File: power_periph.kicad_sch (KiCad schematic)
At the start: 6 parts, among them J6 UART_GPS, J7 UART_ELRS, J9 I2C_MAG

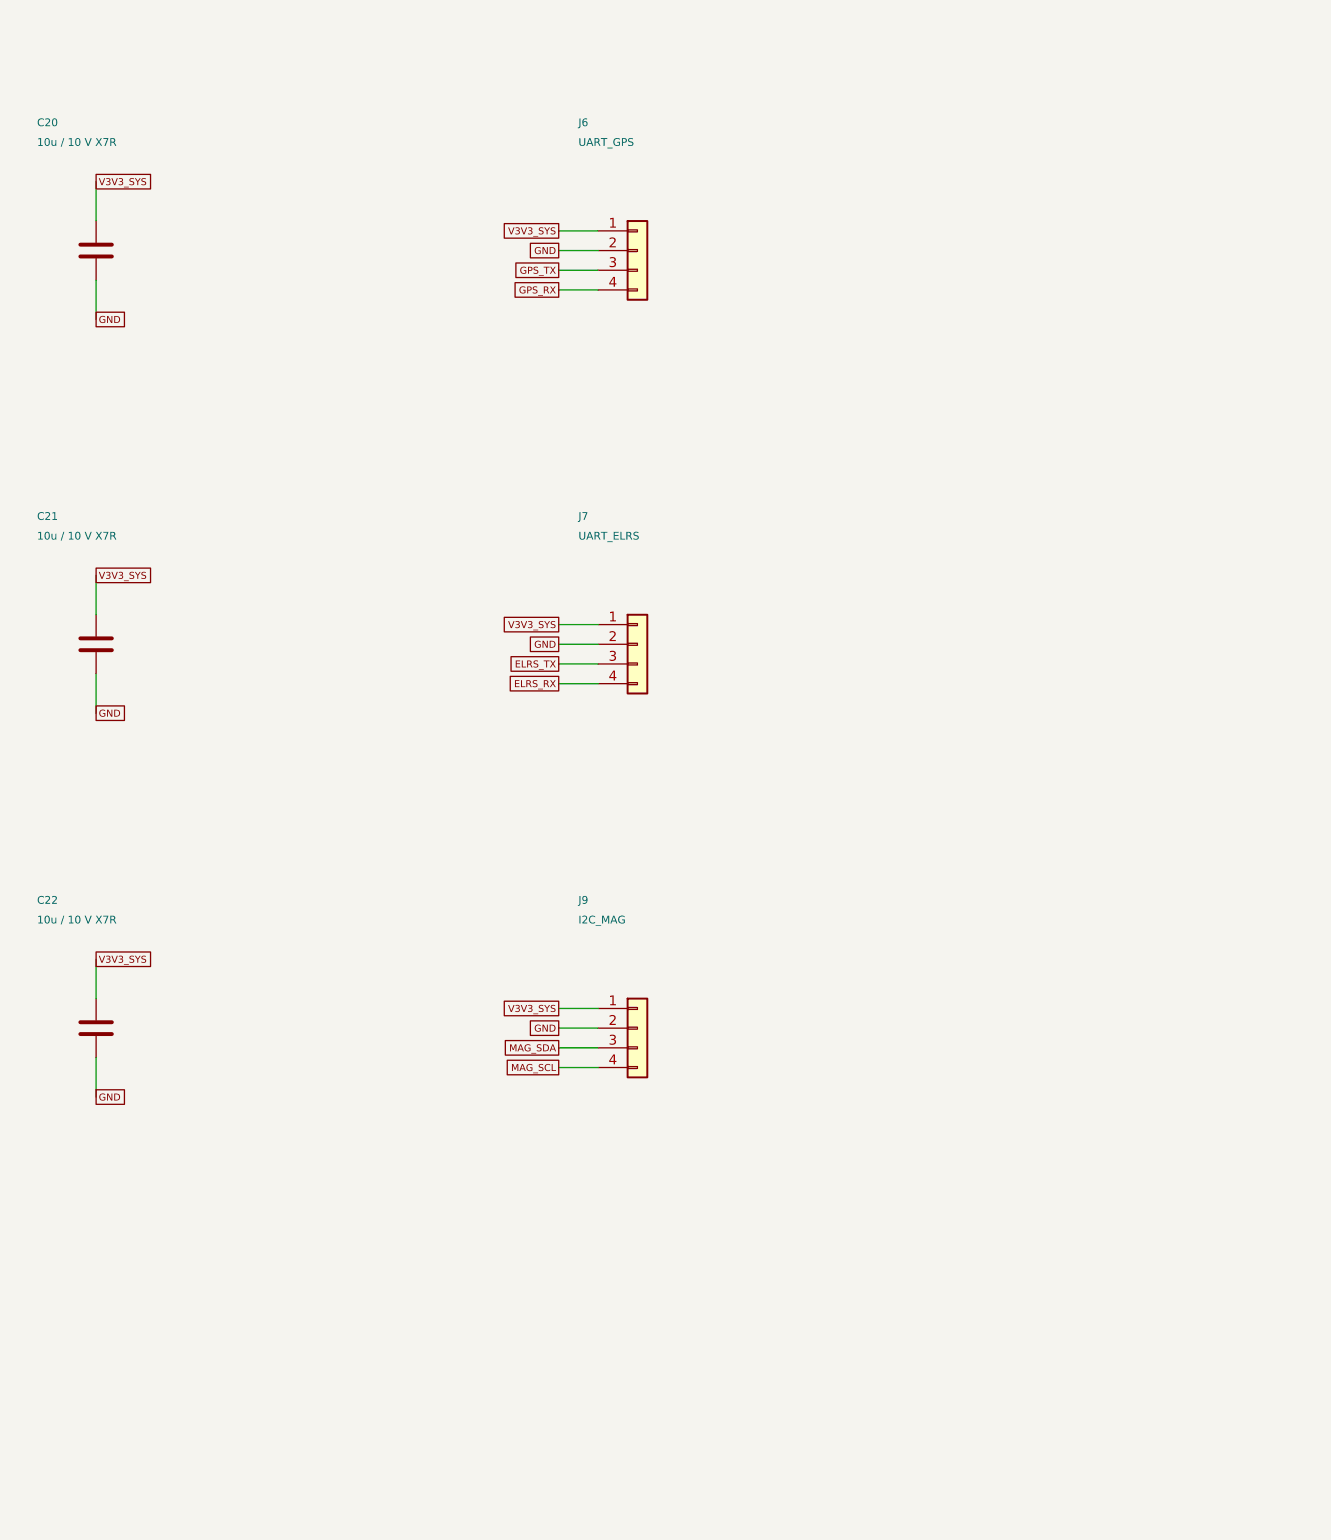
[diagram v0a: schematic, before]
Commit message: Schematic review: TPS2121 input stage, DS-009 ports, sequencing and CS fixes; docs trimmed
Datasheet-grounded review of the full flight-controller schematic. Downstream
of the input everything verified pin-by-pin (TPS62913, TPS7A20, RP2354B,
BMI088/BMP581/ADXL375, W25Q128, microSD, PWM). The 5 V input stage did not:

- LM66100 (5.5 V rec-op / 6 V abs-max) replaced by one TPS2121 mux (U25):
  BEC priority on IN1, OV lockout ~5.86 V, current limit ~1.5 A, reverse
  blocking on both inputs, source status on GPIO39. Input spec 4.75-5.5 V.
- 5V_IN: 2x4.7 uF + 100 uF + SMAJ5.0A TVS; J3 JST-XH -> XT30PW-M (pin 1 GND).
- J6/J7/J9 reordered to Pixhawk DS-009 (VCC/sig/sig/GND); GPS/ELRS VCC 5 V.
- VIN_SENSE 22k/10k (full scale 10.6 V, was saturating at 5.5 V).
- TPS7A20 EN <- PWR_GOOD so V3V3_ANA rises after V3V3_SYS.
- RP2354B VREG_AVDD moved to V3V3_SYS (datasheet 6.1.8: must power up with
  VREG_VIN); ADC_AVDD stays on V3V3_ANA.
- 10k pull-ups on the four sensor chip-selects.
- ERC "global label appears once" re-enabled (0 hits).

Generator, netlist checker and SPICE decks updated (TPS2121 behavioral model,
new over-voltage and 2S mis-plug corners). Build idempotent, 143 pin mappings
PASS, ERC 0/0, all corners PASS.

Docs: POWER_*.md history removed, rationale folded into DESIGN_SPEC Decisions;
808 -> 290 lines across README, DESIGN_SPEC, LIBRARIES, simulations/README.

Co-Authored-By: Claude Fable 5.1 <noreply@anthropic.com>
Claude-Session: https://claude.ai/code/session_015cFNiWgf35VN2T43HaK8PE
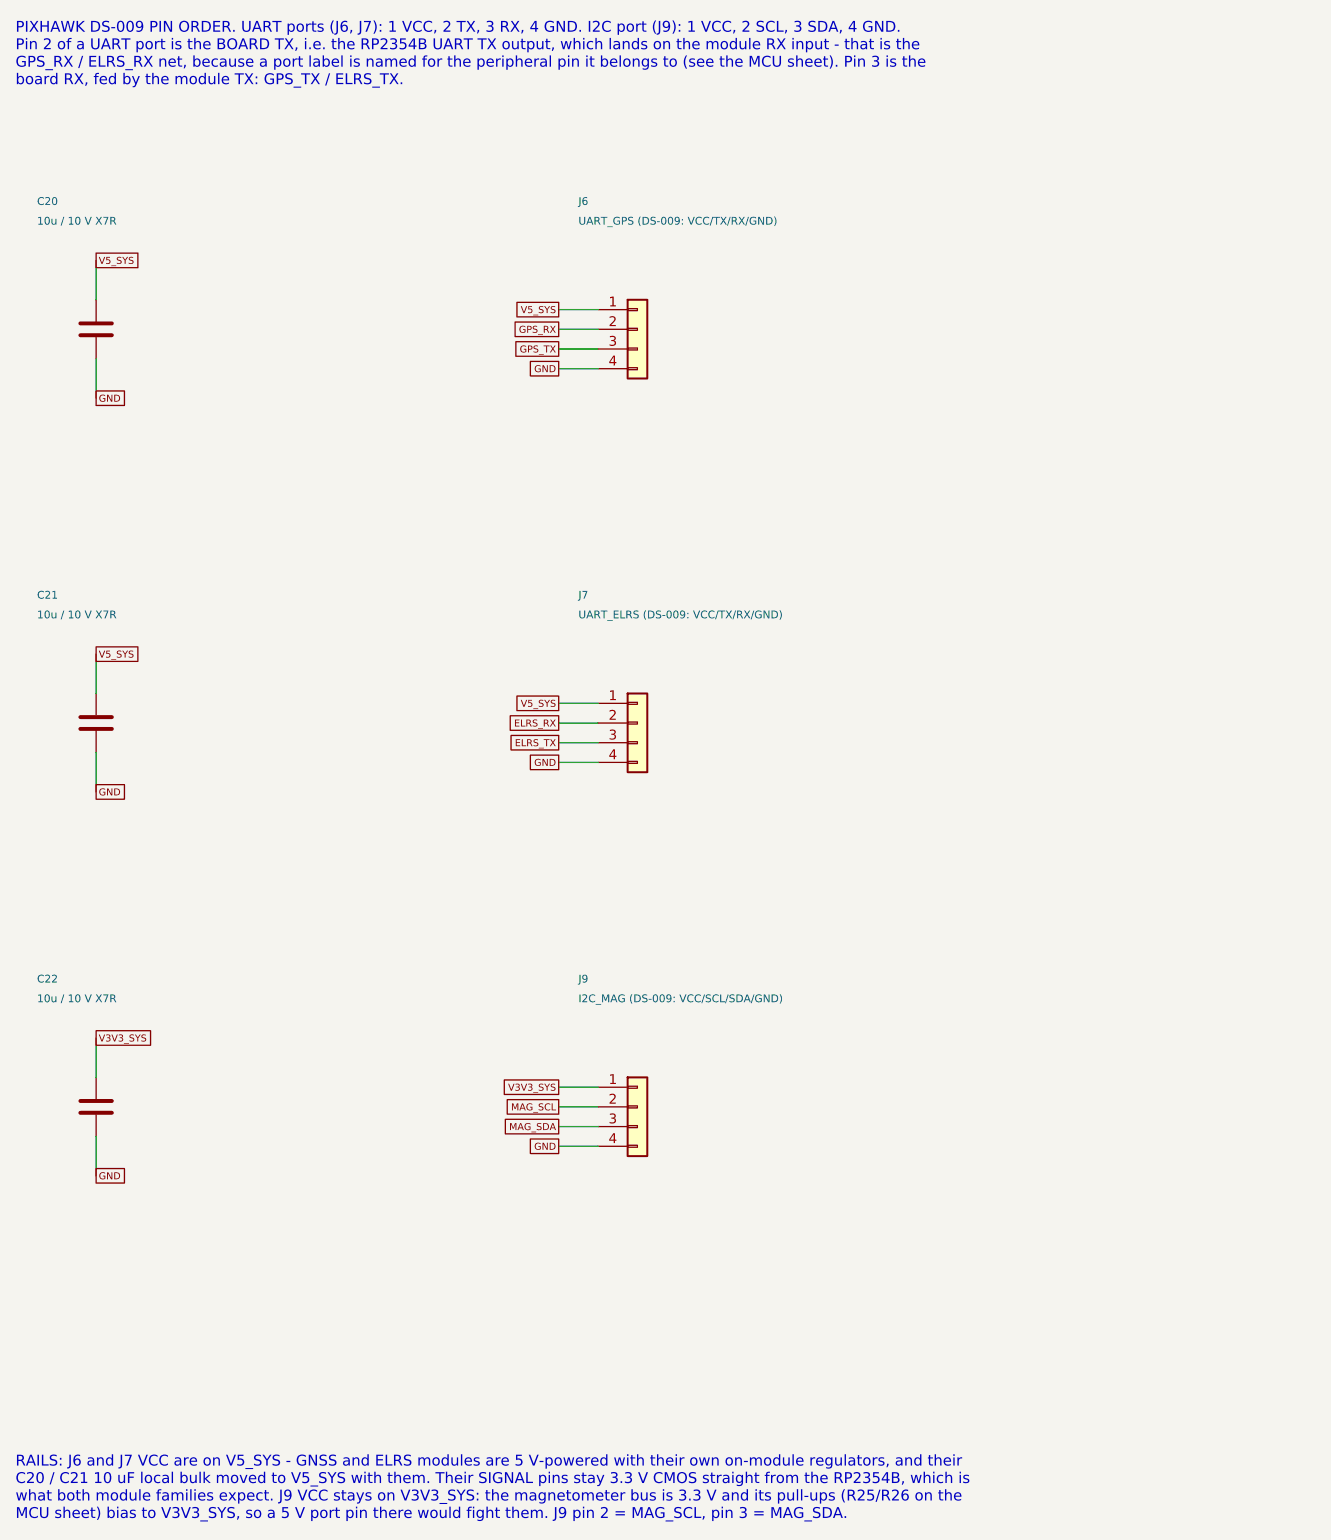
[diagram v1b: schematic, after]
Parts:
- J6: value UART_GPS -> UART_GPS (DS-009: VCC/TX/RX/GND)
- J7: value UART_ELRS -> UART_ELRS (DS-009: VCC/TX/RX/GND)
- J9: value I2C_MAG -> I2C_MAG (DS-009: VCC/SCL/SDA/GND)
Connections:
- net ELRS_RX: now also J7.2 (Pin_2); no longer J7.4 (Pin_4)
- net GND: now also J6.4 (Pin_4), J7.4 (Pin_4), J9.4 (Pin_4); no longer J6.2 (Pin_2), J7.2 (Pin_2), J9.2 (Pin_2)
- net GPS_RX: now also J6.2 (Pin_2); no longer J6.4 (Pin_4)
- net MAG_SCL: now also J9.2 (Pin_2); no longer J9.4 (Pin_4)
- net V3V3_SYS: no longer C20.1, C21.1, J6.1 (Pin_1), J7.1 (Pin_1)
- new net V5_SYS: C20.1, C21.1, J6.1 (Pin_1), J7.1 (Pin_1)
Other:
- note added: "PIXHAWK DS-009 PIN ORDER. UART ports (J6, J7): 1 VCC, 2 TX, 3 RX, 4 GND. I2C port (J9): 1 VCC, 2 SCL, 3 SDA, 4 GND. Pin 2 of a UART port is the BOARD TX, i.e. the RP2354B UART TX output, which lands on the module RX input - that is the GPS_RX / ELRS_RX net, because a port label is named for the peripheral pin it belongs to (see the MCU sheet). Pin 3 is the board RX, fed by the module TX: GPS_TX /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"
- note added: "RAILS: J6 and J7 VCC are on V5_SYS - GNSS and ELRS modules are 5 V-powered with their own on-module regulators, and their C20 / C21 10 uF local bulk moved to V5_SYS with them. Their SIGNAL pins stay 3.3 V CMOS straight from the RP2354B, which is what both module families expect. J9 VCC stays on V3V3_SYS: the magnetometer bus is 3.3 V and its pull-ups (R25/R26 on the MCU sheet) bias to V3V3_SYS, s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"
- moved on the sheet: C20, C21, C22, J6, J7, J9

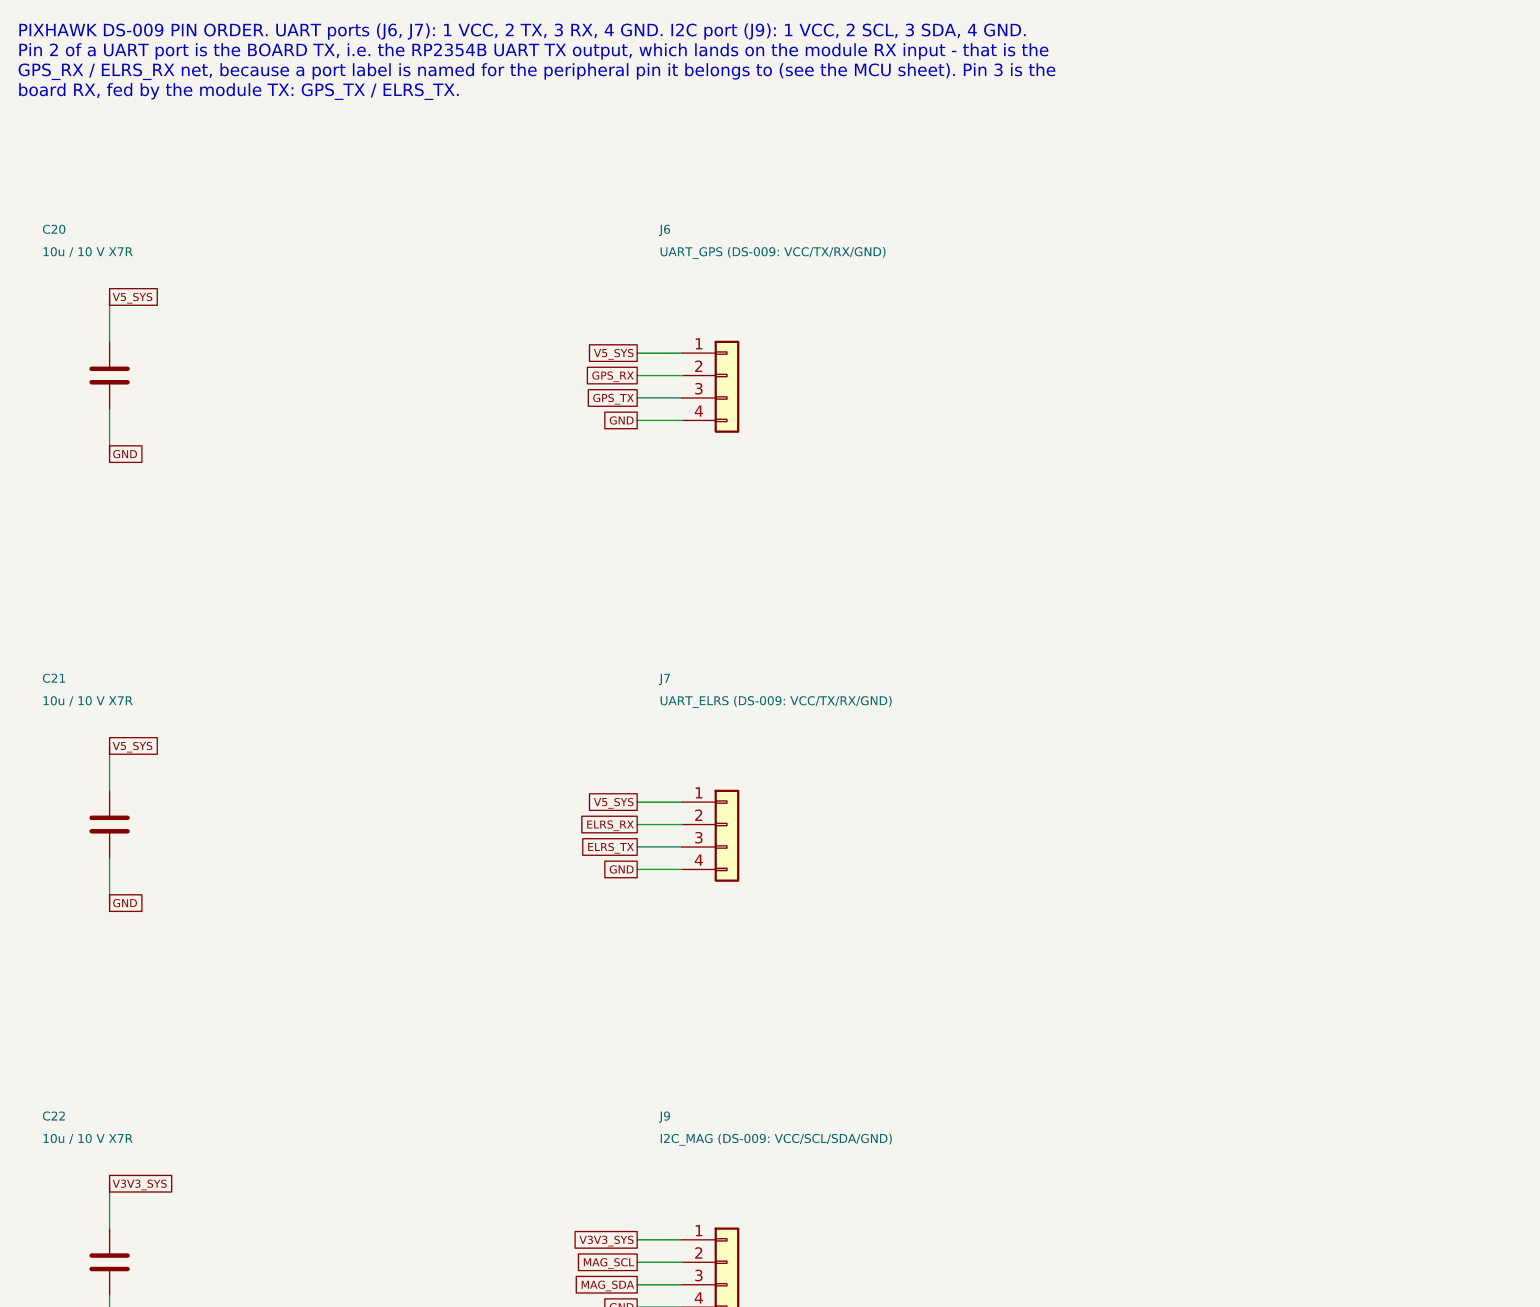
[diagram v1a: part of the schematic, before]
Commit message: Physical design: VBAT-in buck, ESC pad row, pad-row IO, 50 mm single-sided board
Power: the FC now takes raw 2-6S VBAT from the MicoAir AM32 4-in-1 ESC pad
row (CURR TX M4 M3 M2 M1 VBAT GND, J3) through an AP63205WU 5 V/2 A buck
(U26, XGL4030-472, 3 x 22 uF) into the existing TPS2121 mux; XT30 and its
TVS removed. VBAT sense 100k/10k (36 V FS) on ADC0, ESC current sense on
ADC2, ESC KISS telemetry on GPIO30.

IO per the physical spec (DESIGN_SPEC "Physical design"): solder pad rows
for GPS/ELRS/MAG (JST-GH removed), DBG and buzzer; 3x4 servo block for
PWM5-8; 2x6 spare-IO block; WS2812C-2020 RGB LED replaces the two discrete
LEDs; buzzer moved off-board to pads; flash socket is the 150-mil SOIC-8
(W25Q64 default, APS6404L PSRAM alternative); four 4.0 mm grommet holes on
the 30.5 mm pattern. Passives moved to 0402/0603 for the single-sided
envelope.

Board: tools/setup_pcb.py regenerates MARV-V2.kicad_pcb from the netlist —
50 x 50 mm, 4-layer JLC 7628 stack-up, net classes incl. a 90 ohm USB pair,
edge-anchored connectors, coarse interior placement, silk pad labels.
DRC leaves only unrouted items. The BMP581 project footprint had its 2-pad
edges at +/-0.5 mm (corner pads overlapped, three nets shorted); corrected
to Bosch Fig. 32 (+/-0.25 mm, 0.20 mm gaps).

Checks: ERC 0/0, 217 pin mappings / 139 components, run_power_checks PASS,
audit 139/139, pcb DRC unrouted-only.

Co-Authored-By: Claude Fable 5.1 <noreply@anthropic.com>
Claude-Session: https://claude.ai/code/session_01U6Ud7JA3CDTJZVcZZr5sx1
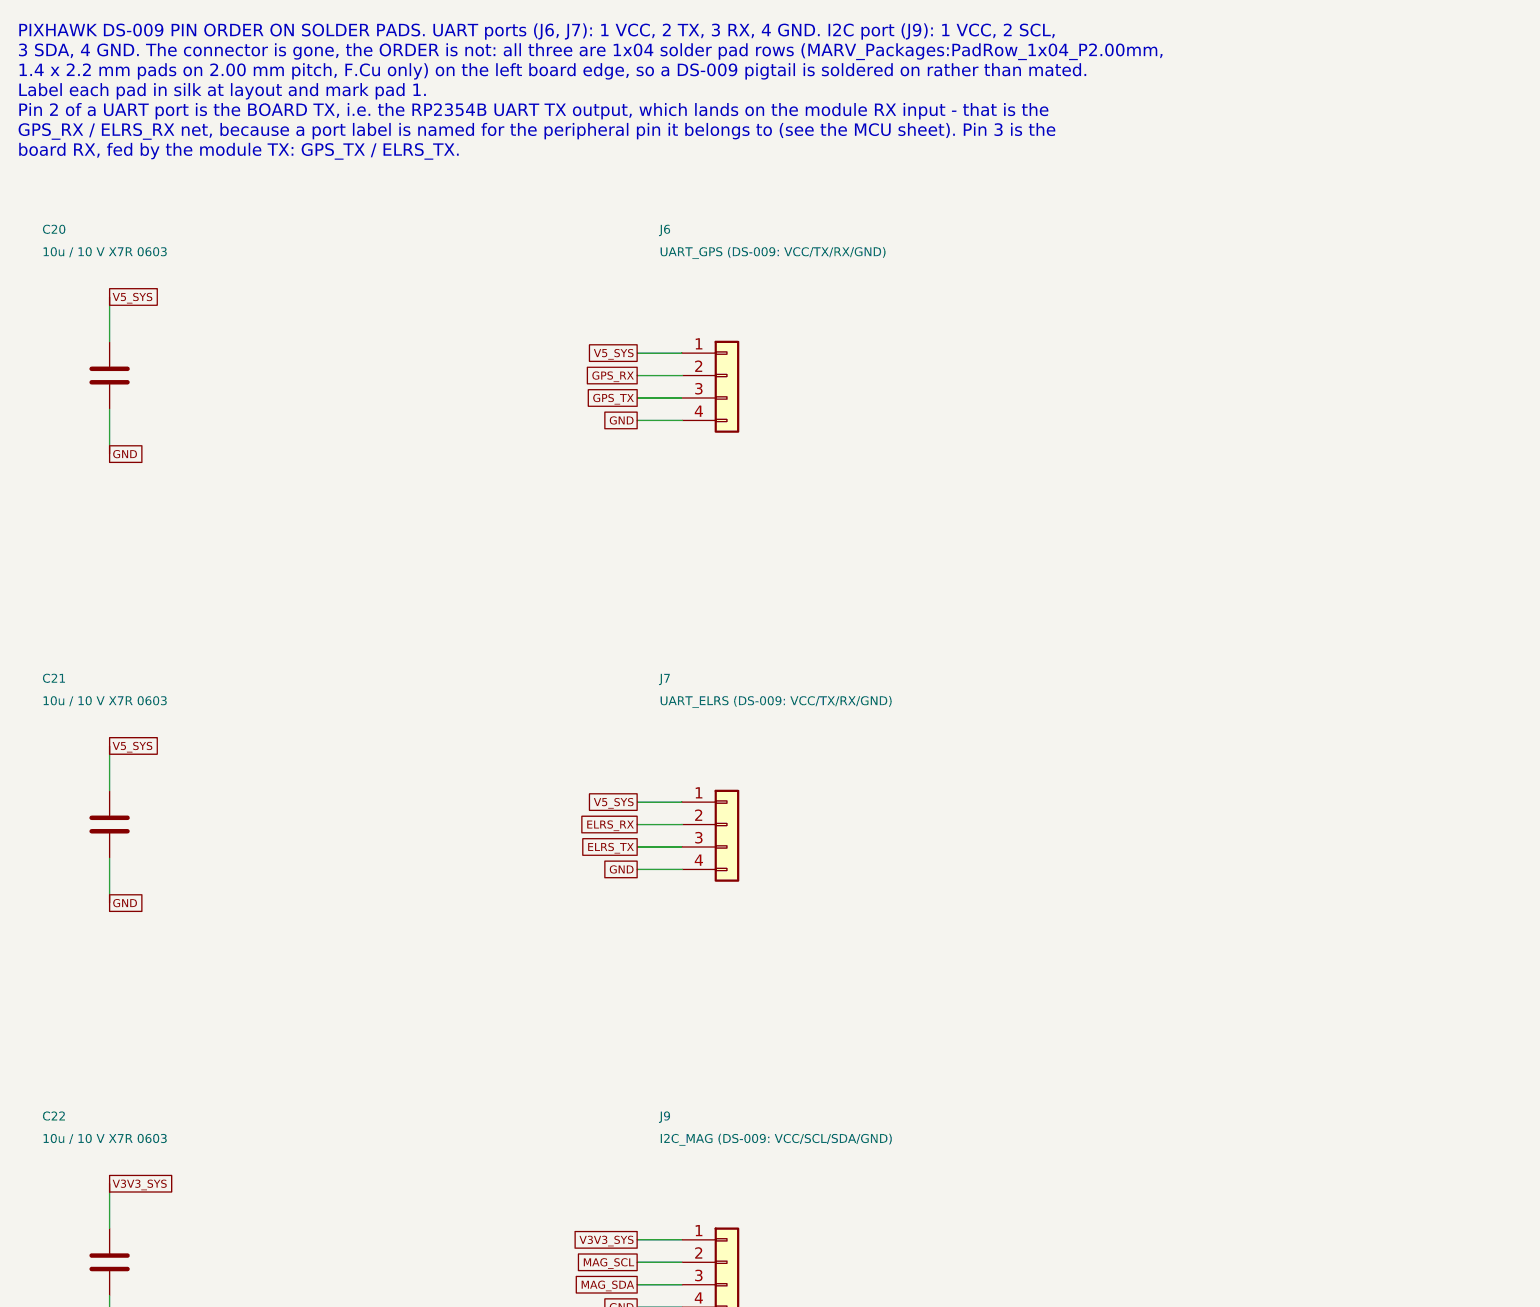
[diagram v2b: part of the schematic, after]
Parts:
- C20, C21, C22: value 10u / 10 V X7R -> 10u / 10 V X7R 0603; footprint Capacitor_SMD:C_0805_2012Metric -> Capacitor_SMD:C_0603_1608Metric
- J6, J7, J9: footprint Connector_JST:JST_GH_SM04B-GHS-TB_1x04-1MP_P1.25mm_Horizontal -> MARV_Packages:PadRow_1x04_P2.00mm
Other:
- note added: "PIXHAWK DS-009 PIN ORDER ON SOLDER PADS. UART ports (J6, J7): 1 VCC, 2 TX, 3 RX, 4 GND. I2C port (J9): 1 VCC, 2 SCL, 3 SDA, 4 GND. The connector is gone, the ORDER is not: all three are 1x04 solder pad rows (MARV_Packages:PadRow_1x04_P2.00mm, 1.4 x 2.2 mm pads on 2.00 mm pitch, F.Cu only) on the left board edge, so a DS-009 pigtail is soldered on rather than mated. Label each pad in silk at layou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"
- note removed: "PIXHAWK DS-009 PIN ORDER. UART ports (J6, J7): 1 VCC, 2 TX, 3 RX, 4 GND. I2C port (J9): 1 VCC, 2 SCL, 3 SDA, 4 GND. Pin 2 of a UART port is the BOARD TX, i.e. the RP2354B UART TX output, which lands on the module RX input - that is the GPS_RX / ELRS_RX net, because a port label is named for the peripheral pin it belongs to (see the MCU sheet). Pin 3 is the board RX, fed by the module TX: GPS_TX /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"
